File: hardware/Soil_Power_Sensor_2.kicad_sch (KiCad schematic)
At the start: 4 parts, among them J1 Conn_01x02, SW3 SW_SPDT

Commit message: usb ttl components
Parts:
- added BT1, BT2: 3.7 V 2.2 Ah Li-ion 18650, footprints:MY-18650-02, symbol Device:Battery_Cell
- added C10, C18: 10uF, Capacitor_SMD:C_0603_1608Metric, symbol Device:C
- added C11, C17: 100nF, Capacitor_SMD:C_0603_1608Metric, symbol Device:C
- added C3, C4: 1 uF, Capacitor_SMD:C_0603_1608Metric, symbol Device:C_Polarized_Small_US
- added C9: 47 uF, Capacitor_SMD:C_0603_1608Metric, symbol Device:C_Polarized_Small_US
- added D4, D5: LED, LED_SMD:LED_0603_1608Metric, symbol Device:LED
- added F1: 3561KTR, 3561KTR:FUSE_3561KTR, symbol 3561KTR:3561KTR
- added J11: DC050-T, DC050-T:DC050-T, symbol Connector:Barrel_Jack_Switch
- added JP2: SolderJumper_2_Bridged, Jumper:SolderJumper-2_P1.3mm_Bridged_RoundedPad1.0x1.5mm, symbol Jumper:SolderJumper_2_Bridged
- added JP2, JP3, JP8, JP9: SolderJumper_2_Open, Jumper:SolderJumper-2_P1.3mm_Open_RoundedPad1.0x1.5mm, symbol Jumper:SolderJumper_2_Open
- added JP4: Jumper_2_Bridged, symbol Jumper:Jumper_2_Bridged
- added R18: 7.32 kOhm, Resistor_SMD:R_0603_1608Metric, symbol Device:R_Small_US
- added R21: 680 Ohm, Resistor_SMD:R_0603_1608Metric, symbol Device:R_Small_US
- added R6, R7: 2 kOhm, Resistor_SMD:R_0603_1608Metric, symbol Device:R_Small_US
- added R8, R9: 1 MOhm, Resistor_SMD:R_0603_1608Metric, symbol Device:R_Small_US
- added RT1: 21.5 kOhm, Resistor_SMD:R_0603_1608Metric, symbol Device:R_Small_US
- added S1: PCM12SMTR, Button_Switch_SMD:SW_SPDT_PCM12, symbol JS102011SAQN:JS102011SAQN
- added TH1: 103AT NTC, Connector_PinHeader_2.54mm:PinHeader_1x02_P2.54mm_Vertical, symbol Device:Thermistor_NTC_US
- added TP1: Vin, TestPoint:TestPoint_Pad_D1.5mm, symbol Connector:TestPoint
- added TP2: VBAT sense, TestPoint:TestPoint_Pad_D1.5mm, symbol Connector:TestPoint
- added U2: BQ24210DQCR, BQ24210:DQC10_P84X2P4, symbol BQ24210:BQ24210DQCR
- added U5: XC6210B332MR, Package_TO_SOT_SMD:SOT-23-5, symbol Regulator_Linear:XC6210B332MR
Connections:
- net GND: now also C10.2, C11.2, C17.2, C18.2, C9.2, U5.2 (GND)
- net VBAT/2: now also R8.2, R9.1, TP2.1
- net ~{CHG}: now also JP2.1 (A), U2.8 (~{CHG})
- net ~{PG}: now also JP2.1 (A), JP3.1 (A), U2.6 (~{PG})
- new net: C4.1, F1.2, JP8.2 (B), R6.1, R7.1, S1.2, U2.10 (BAT)
- new net: C17.1, C18.1, S1.1, U5.1 (VIN), U5.3 (CE)
- new net: C10.1, C11.1, C9.1, JP4.1 (A), U5.5 (VOUT)
- new net: D4.1 (K), JP2.2 (B)
- new net: D4.2 (A), R6.2
- new net: RT1.1, U2.4 (VTSB)
- new net: RT1.2, TH1.1, U2.5 (TS)
- new net: JP2.2 (B), U2.7 (~{EN})
- new net: C3.1, J11.1, TP1.1, U2.1 (VBUS)
- new net: BT1.1 (+), BT2.1 (+), F1.1, JP8.1 (A)
- new net: D5.1 (K), JP3.2 (B)
- new net: D5.2 (A), R7.2
- new net: JP9.1 (A), R8.1
- new net: R18.1, U2.9 (VDPM)
- new net: R21.1, U2.2 (ISET)
- new net +3V3: JP4.2 (B)
- new net 0: BT1.2 (-), BT2.2 (-), C3.2, C4.2, J11.2, R18.2, R21.2, R9.2, TH1.2, U2.11 (EPAD), U2.3 (VSS)
- no-connect marks 2 -> 4
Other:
- note added: "15-23 mV dropout @ 30 mA 50-70 mV dropout @ 100 mA"
- note added: "RT1 = (1/V_{V45C}) * RTH(45C) - RTH(45C) = (1/0.186) * 5000 - 5000 = 21.881 kOhm approx 21.5 kOhm"
- note added: "R_{ISET} = K_{ISET} / I_{OUT} K_{ISET} typical 395 amp-ohm I_{OUT} from 50 mA to 800 mA R_{ISET} 500 ohm --> I_{OUT} ~800 mA R_{ISET} 680 ohm --> I_{OUT} ~580 mA min 675 max 10.8k"
- note added: "TH1 footprint is just 2 holes since TH1 needs to be attached to the battery."
- note added: "VCC or 3V3?"
- note added: "VDPM left floating to use battery tracking mode, can be between 1k 10k"
- note added: "~{EN} tied to ~{PG} to auto-enable charge and disable load mode"

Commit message: john pcb review feedback
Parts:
- removed BT1, BT2: 3.7 V 2.2 Ah Li-ion 18650, footprints:MY-18650-02, symbol Device:Battery_Cell
- removed F1: 3561KTR, 3561KTR:FUSE_3561KTR, symbol 3561KTR:3561KTR
- removed S1: PCM12SMTR, Button_Switch_SMD:SW_SPDT_PCM12, symbol JS102011SAQN:JS102011SAQN
- removed SW3: SW_SPDT, Soil Power Sensor:JS102011SCQN, symbol Switch:SW_SPDT
- added D11, D12: D, symbol Device:D
- added F3: Polyfuse, symbol Device:Polyfuse
- added Q10, Q8: AO3401A, Package_TO_SOT_SMD:SOT-23, symbol Simulation_SPICE:PMOS
- added Q9: BSS123, Package_TO_SOT_SMD:SOT-23, symbol Transistor_FET:BSS123
- added R40, R43, R45: 470k, Resistor_SMD:R_0603_1608Metric, symbol Device:R
- added R41, R42, R44: 10k, Resistor_SMD:R_0603_1608Metric, symbol Device:R
- JP1: renamed from JP4; footprint (none) -> Connector_PinHeader_2.54mm:PinHeader_1x02_P2.54mm_Vertical
- R7: renamed from R18; now fitted
- renumbered C3 to C1, C4 to C2, C17 to C3, C18 to C4, C11 to C5, C10 to C6, C9 to C7, D4 to D1, D5 to D2, J11 to J2, JP9 to JP4, JP2 to JP5, JP8 to JP6, R16 to R1, R17 to R2, R6 to R3, R7 to R4, R8 to R5, R9 to R6, R21 to R8, U2 to U1, U5 to U2
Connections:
- net 0: now also Q9.2 (S); no longer R7.2
- net GND: now also R40.2, R43.2, R45.2
- net VBAT: now also JP6.1 (A), F3.2
- net VCC: now also C3.1, C4.1, U2.1 (VIN), U2.3 (CE), D12.1 (K), Q10.1 (D)
- net VUSB: now also D11.2 (A), D12.2 (A), R41.2, R42.2, R44.2
- net at C2.1, JP6.2 (B), R3.1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: now also F3.1, Q10.3 (S)
- net at C1.1, TP1.1, U1.1 (VBUS): now also D11.1 (K), Q8.1 (D); no longer J2.1
- new net: Q10.2 (G), R44.1, R45.1
- new net: J2.1, Q8.3 (S)
- new net: Q8.2 (G), R40.1, R41.1
- new net: Q9.1 (G), R42.1, R43.1
- new net: Q9.3 (D), R7.2
- no-connect marks 4 -> 2
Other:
- note added: "CHECK FOOTPRINT OF ALL MOSFETS"
- note added: "PG AND CHG AND OTHER INDICATORS TO GPIO EXPANDER"
- note added: "coin cell RTC"
- note removed: "VCC or 3V3?"
- note removed: "todo: move battery baord LDOs and solar charging circuit here"
- moved on the sheet: C1, C7, J1, JP4, R1, R2, R5, R6, TH1, TP2

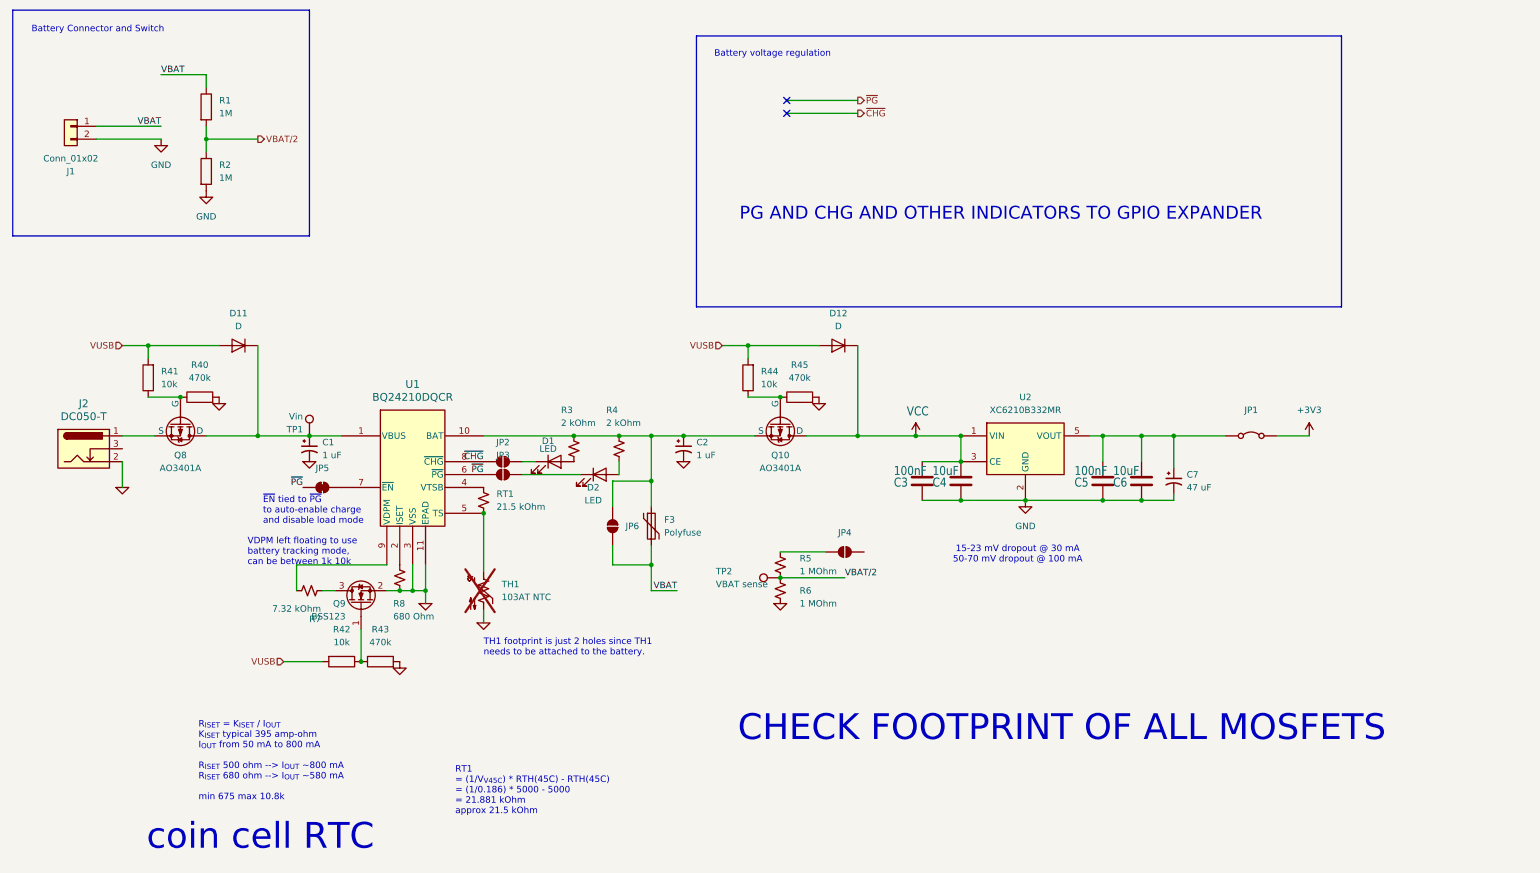
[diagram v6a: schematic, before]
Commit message: buck-boost TPS631000
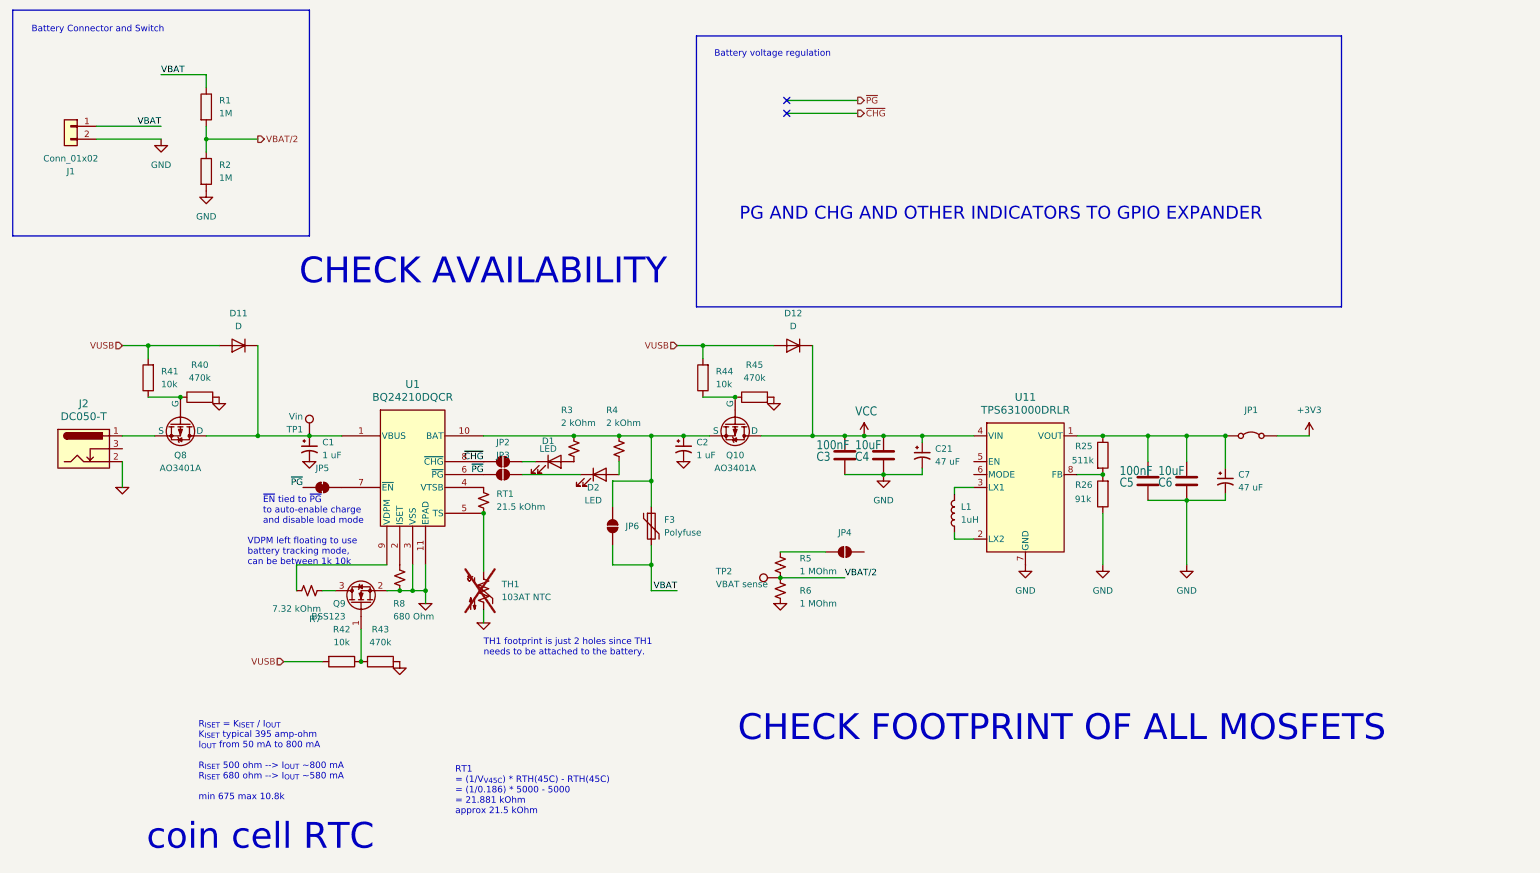
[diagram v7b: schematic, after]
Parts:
- removed U2: XC6210B332MR, Package_TO_SOT_SMD:SOT-23-5, symbol Regulator_Linear:XC6210B332MR
- added C21: 47 uF, Capacitor_SMD:C_0603_1608Metric, symbol Device:C_Polarized_Small_US
- added L1: 1uH, symbol Device:L
- added R25: 511k, Resistor_SMD:R_0603_1608Metri, symbol Device:R
- added R26: 91k, Resistor_SMD:R_0603_1608Metric, symbol Device:R
- added U11: TPS631000DRLR, Soil Power Sensor:TPS631000DRLR_TEX, symbol Soil Power Sensor-eagle-import:TPS631000DRLR
- JP2, JP3, JP4, JP5, JP6: now in the parts list
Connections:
- net GND: now also C21.2, R26.1, U11.7 (GND)
- net VCC: now also C21.1, U11.4 (VIN)
- net at C5.1, C6.1, C7.1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: now also R25.1, U11.1 (VOUT)
- new net: R25.2, R26.2, U11.8 (FB)
- new net: L1.1, U11.3 (LX1)
- new net: L1.2, U11.2 (LX2)
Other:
- note added: "CHECK AVAILABILITY"
- note removed: "15-23 mV dropout @ 30 mA 50-70 mV dropout @ 100 mA"
- moved on the sheet: C3, C4, C5, C6, C7, D12, Q10, R44, R45

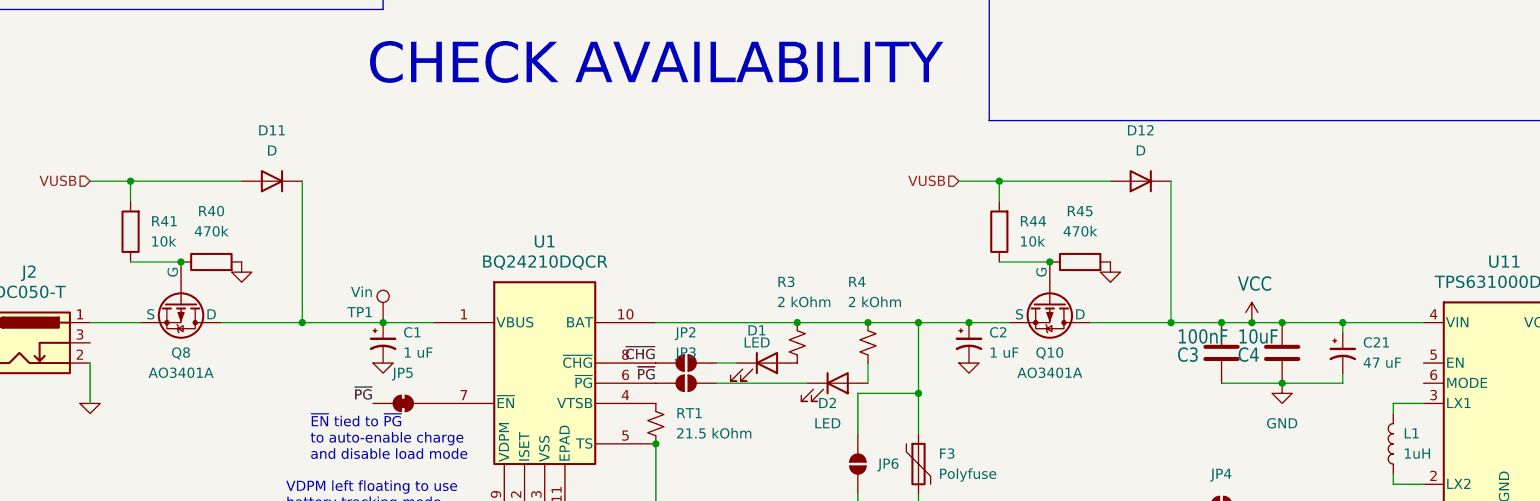
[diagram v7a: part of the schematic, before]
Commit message: pcb outline
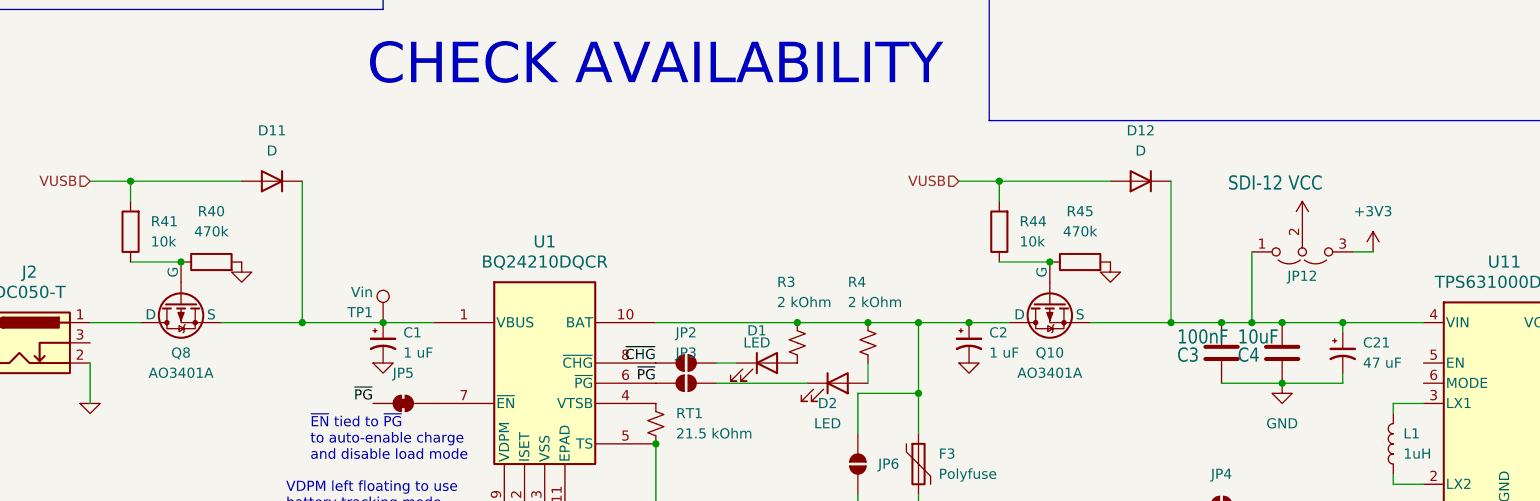
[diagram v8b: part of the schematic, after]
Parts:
- added JP12: Jumper_3_Open, Connector_PinHeader_2.54mm:PinHeader_1x03_P2.54mm_Vertical, symbol Jumper:Jumper_3_Open
- D11, D12: footprint (none) -> Diode_SMD:D_0603_1608Metric
- F3: footprint (none) -> Fuse:Fuse_0603_1608Metric
- J2: footprint DC050-T:DC050-T -> Connector_BarrelJack:BarrelJack_Horizontal
- L1: footprint (none) -> Inductor_SMD:L_0805_2012Metric
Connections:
- net +3V3: now also JP12.3 (B)
- net at C2.1, F3.1, JP6.2 (B)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: now also Q10.1 (D); no longer Q10.3 (S)
- net at J2.1: now also Q8.1 (D); no longer Q8.3 (S)
- net at C1.1, D11.1 (K), TP1.1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: now also Q8.3 (S); no longer Q8.1 (D)
- net VCC: no longer names the net of C21.1, C3.1, C4.1, D12.1 (K), U11.4 (VIN)
- net VCC: now also Q10.3 (S), JP12.1 (A); no longer Q10.1 (D)
- new net SDI-12 VCC: JP12.2 (C)
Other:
- moved on the sheet: Q10, Q8
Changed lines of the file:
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@@
 	)
 	(junction
-		(at 180.34 96.52)
-		(diameter 0)
-		(color 0 0 0 0)
-	)
-	(junction
 		(at 184.15 96.52)
 		(diameter 0)
@@
 	)
 	(junction
+		(at 180.34 96.52)
+		(diameter 0)
+		(color 0 0 0 0)
+	)
+	(junction
 		(at 81.28 140.97)
 		(diameter 0)
@@
 	(wire
 		(pts
-			(xy 180.34 96.52) (xy 184.15 96.52)
+			(xy 176.53 96.52) (xy 180.34 96.52)
 		)
 		(stroke
@@
 	(wire
 		(pts
+			(xy 180.34 87.63) (xy 180.34 96.52)
+		)
+		(stroke
+			(width 0)
+			(type default)
+		)
+	)
+	(wire
+		(pts
 			(xy 198.12 115.57) (xy 198.12 116.84)
 		)
@@
 	(wire
 		(pts
+			(xy 180.34 96.52) (xy 184.15 96.52)
+		)
+		(stroke
+			(width 0)
+			(type default)
+		)
+	)
+	(wire
+		(pts
 			(xy 243.84 96.52) (xy 251.46 96.52)
 		)
@@
 	(wire
 		(pts
-			(xy 176.53 96.52) (xy 180.34 96.52)
-		)
-		(stroke
-			(width 0)
-			(type default)
-		)
-	)
-	(wire
-		(pts
 			(xy 29.21 38.1) (xy 41.91 38.1)
 		)
@@
 	(wire
 		(pts
+			(xy 195.58 87.63) (xy 193.04 87.63)
+		)
+		(stroke
+			(width 0)
+			(type default)
+		)
+	)
+	(wire
+		(pts
 			(xy 50.8 35.56) (xy 50.8 38.1)
 		)
@@
 	)
 	(symbol
+		(lib_id "power:+3V3")
+		(at 195.58 87.63 0)
+		(unit 1)
+		(exclude_from_sim no)
+		(in_bom yes)
+		(on_board yes)
+		(dnp no)
+		(property "Reference" "#PWR055"
+			(at 195.58 91.44 0)
+			(effects
+				(font
+					(size 1.27 1.27)
+				)
+				(hide yes)
+			)
+		)
+		(property "Value" "+3V3"
+			(at 195.58 82.55 0)
+			(effects
+				(font
+					(size 1.27 1.27)
+				)
+			)
+		)
+		(property "Footprint" ""
+			(at 195.58 87.63 0)
+			(effects
+				(font
+					(size 1.27 1.27)
+				)
+				(hide yes)
+			)
+		)
+		(property "Datasheet" ""
+			(at 195.58 87.63 0)
+			(effects
+				(font
+					(size 1.27 1.27)
+				)
+				(hide yes)
+			)
+		)
+		(property "Description" "Power symbol creates a global label with name \"+3V3\""
+			(at 195.58 87.63 0)
+			(effects
+				(font
+					(size 1.27 1.27)
+				)
+				(hide yes)
+			)
+		)
+		(pin "1"
+		)
+		(instances
+			(project "Soil Power Sensor"
+				(path "/5300ec4d-4648-40a1-8d89-4fa6b3bf32a3/642281e5-1644-4dc3-b6e5-bcf5b1c03ff1"
+					(reference "#PWR055")
+					(unit 1)
+				)
+			)
+		)
+	)
+	(symbol
 		(lib_id "Device:C")
 		(at 236.22 105.41 0)
@@
 	(symbol
 		(lib_id "Simulation_SPICE:PMOS")
-		(at 154.94 93.98 270)
+		(at 154.94 93.98 90)
+		(mirror x)
 		(unit 1)
 		(exclude_from_sim no)
@@
 		(on_board yes)
 		(dnp no)
-		(fields_autoplaced yes)
 		(property "Reference" "Q10"
 			(at 154.94 100.33 90)
@@
 		)
 		(property "Footprint" "Package_TO_SOT_SMD:SOT-23"
-			(at 157.48 99.06 0)
+			(at 152.4 99.06 0)
 			(effects
 				(font
@@
 		)
 		(property "Datasheet" "https://mm.digikey.com/Volume0/opasdata/d220001/medias/docus/2969/UMW%20AO3401A.pdf"
-			(at 142.24 93.98 0)
+			(at 167.64 93.98 0)
 			(effects
 				(font
@@
 		)
 		(property "Sim.Device" "PMOS"
-			(at 137.795 93.98 0)
+			(at 172.085 93.98 0)
 			(effects
 				(font
@@
 		)
 		(property "Sim.Type" "VDMOS"
-			(at 135.89 93.98 0)
+			(at 173.99 93.98 0)
 			(effects
 				(font
@@
 		)
 		(property "Sim.Pins" "1=D 2=G 3=S"
-			(at 139.7 93.98 0)
+			(at 170.18 93.98 0)
 			(effects
 				(font
@@
 			)
 		)
-		(property "Footprint" "DC050-T:DC050-T"
+		(property "Footprint" "Connector_BarrelJack:BarrelJack_Horizontal"
 			(at 27.94 100.076 0)
 			(effects
@@
 			)
 		)
-		(property "Footprint" ""
+		(property "Footprint" "Diode_SMD:D_0603_1608Metric"
 			(at 57.15 78.74 0)
 			(effects
@@
 	)
 	(symbol
+		(lib_id "Jumper:Jumper_3_Open")
+		(at 186.69 87.63 0)
+		(mirror x)
+		(unit 1)
+		(exclude_from_sim no)
+		(in_bom no)
+		(on_board yes)
+		(dnp no)
+		(property "Reference" "JP12"
+			(at 186.69 90.678 0)
+			(effects
+				(font
+					(size 1.27 1.27)
+				)
+			)
+		)
+		(property "Value" "Jumper_3_Open"
+			(at 186.69 92.202 0)
+			(effects
+				(font
+					(size 1.27 1.27)
+				)
+				(hide yes)
+			)
+		)
+		(property "Footprint" "Connector_PinHeader_2.54mm:PinHeader_1x03_P2.54mm_Vertical"
+			(at 186.69 87.63 0)
+			(effects
+				(font
+					(size 1.27 1.27)
+				)
+				(hide yes)
+			)
+		)
+		(property "Datasheet" "~"
+			(at 186.69 87.63 0)
+			(effects
+				(font
+					(size 1.27 1.27)
+				)
+				(hide yes)
+			)
+		)
+		(property "Description" "Jumper, 3-pole, both open"
+			(at 186.69 87.63 0)
+			(effects
+				(font
+					(size 1.27 1.27)
+				)
+				(hide yes)
+			)
+		)
+		(pin "2"
+		)
+		(pin "3"
+		)
+		(pin "1"
+		)
+		(instances
+			(project "Soil Power Sensor"
+				(path "/5300ec4d-4648-40a1-8d89-4fa6b3bf32a3/642281e5-1644-4dc3-b6e5-bcf5b1c03ff1"
+					(reference "JP12")
+					(unit 1)
+				)
+			)
+		)
+	)
+	(symbol
 		(lib_id "power:GND")
 		(at 53.34 88.9 0)
@@
 			)
 		)
-		(property "Footprint" ""
+		(property "Footprint" "Fuse:Fuse_0603_1608Metric"
 			(at 139.7 119.38 0)
 			(effects
@@
 			)
 		)
-		(property "Footprint" ""
+		(property "Footprint" "Inductor_SMD:L_0805_2012Metric"
 			(at 198.12 111.76 0)
 			(effects
@@
 	(symbol
 		(lib_id "power:VCC")
-		(at 180.34 96.52 0)
+		(at 186.69 83.82 0)
 		(mirror y)
 		(unit 1)
@@
 		(dnp no)
 		(property "Reference" "#P+02"
-			(at 180.34 96.52 0)
+			(at 186.69 83.82 0)
 			(effects
 				(font
@@
 			)
 		)
-		(property "Value" "VCC"
-			(at 182.88 92.71 0)
+		(property "Value" "SDI-12 VCC"
+			(at 189.23 80.01 0)
 			(effects
 				(font
@@
 		)
 		(property "Footprint" ""
-			(at 180.34 96.52 0)
+			(at 186.69 83.82 0)
 			(effects
 				(font
@@
 		)
 		(property "Datasheet" ""
-			(at 180.34 96.52 0)
+			(at 186.69 83.82 0)
 			(effects
 				(font
@@
 		)
 		(property "Description" "Power symbol creates a global label with name \"VCC\""
-			(at 180.34 96.52 0)
+			(at 186.69 83.82 0)
 			(effects
 				(font
@@
 			)
 		)
-		(property "Footprint" ""
+		(property "Footprint" "Diode_SMD:D_0603_1608Metric"
 			(at 166.37 78.74 0)
 			(effects
@@
 	(symbol
 		(lib_id "Simulation_SPICE:PMOS")
-		(at 45.72 93.98 270)
+		(at 45.72 93.98 90)
+		(mirror x)
 		(unit 1)
 		(exclude_from_sim no)
@@
 		(on_board yes)
 		(dnp no)
-		(fields_autoplaced yes)
 		(property "Reference" "Q8"
 			(at 45.72 100.33 90)
@@
 		)
 		(property "Footprint" "Package_TO_SOT_SMD:SOT-23"
-			(at 48.26 99.06 0)
+			(at 43.18 99.06 0)
 			(effects
 				(font
@@
 		)
 		(property "Datasheet" "https://mm.digikey.com/Volume0/opasdata/d220001/medias/docus/2969/UMW%20AO3401A.pdf"
-			(at 33.02 93.98 0)
+			(at 58.42 93.98 0)
 			(effects
 				(font
@@
 		)
 		(property "Sim.Device" "PMOS"
-			(at 28.575 93.98 0)
+			(at 62.865 93.98 0)
 			(effects
 				(font
@@
 		)
 		(property "Sim.Type" "VDMOS"
-			(at 26.67 93.98 0)
+			(at 64.77 93.98 0)
 			(effects
 				(font
@@
 		)
 		(property "Sim.Pins" "1=D 2=G 3=S"
-			(at 30.48 93.98 0)
+			(at 60.96 93.98 0)
 			(effects
 				(font
